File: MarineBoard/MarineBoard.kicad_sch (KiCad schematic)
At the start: 152 parts, among them CN1 MKDSN 1,5/ 2-5,08, CN2 MKDSN 1,5/ 2-5,08, CN3 SM04B-SRSS-TB (LF)(SN), J1 USB_C_Receptacle_USB2.0_16P, J3 Conn_02x09_Top_Bottom, Q1 IPL60R075CFD7, Q2 S8050, Q3 S8050, U1 SY8089A1AAC, U10 PC817C-S, U11 SN65HVD230DR, U12 DB125-3.5-3P-GN-S, U13 DB125-3.5-3P-GN-S, U14 PC817C-S, U15 TC4427EPA, U16 PC817C-S, U17 PC817C-S, U18 INA226, U19 INA226, U2 INA226, U20 SMAJ6.8CA, U3 TPS5430DDA, U4 DB125-3.5-2P-GN-S, U5 DB125-3.5-2P-GN-S, U6 DB125-3.5-2P-GN-S, U7 DB125-3.5-3P-GN-S, U8 ESP32-S3-WROOM-2-N32R16V, U9 DB125-3.5-3P-GN-S

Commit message: MarineBoard: schematic library/component update
Co-Authored-By: Claude Sonnet 5 <noreply@anthropic.com>
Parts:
- removed J3: Conn_02x09_Top_Bottom, Connector_PinHeader_1.27mm:PinHeader_2x09_P1.27mm_Vertical, symbol Connector_Generic:Conn_02x09_Top_Bottom
- added J2: DISP_QSPI_4IN_18P, EasyEDA:FH12-18S-0.5SH_QSPI4IN, symbol EasyEDA:DISP_QSPI_4IN_18P
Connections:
- net +3.3V: now also J2.17 (TP_VDD), J2.2 (VCI)
- net FSPIBL/GPIO18: now also J2.12 (FSPIBL)
- net FSPICLK/GPIO12: now also J2.5 (FSPICLK)
- net FSPICS0/GPIO10: now also J2.4 (FSPICS0)
- net FSPID/GPIO11: now also J2.6 (FSPID)
- net FSPIDC/GPIO21: now also J2.10 (FSPIDC)
- net FSPIHD/GPIO9: now also J2.8 (FSPIHD)
- net FSPIQ/GPIO13: now also J2.7 (FSPIQ)
- net FSPIRST/GPIO17: now also J2.3 (FSPIRST)
- net FSPITE/GPIO42: now also J2.11 (FSPITE)
- net FSPITI/GPIO47: now also J2.13 (FSPITI)
- net FSPIWP/GPIO14: now also J2.9 (FSPIWP)
- net GND: now also J2.1 (GND), J2.18 (GND)
- net GPIO3: now also J2.16 (TP_RST)
- net SCL: now also J2.15 (SCL)
- net SDA: now also J2.14 (SDA)

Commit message: MarineBoard: new from-scratch layout; Quilter-compatible footprints
- LCSC: nickname on all EasyEDA footprint lib IDs (board + schematic)
- EasyEDA.pretty upgraded to current KiCad format; 3D models moved to Lib/Models
- U10 FPC mounting tabs numbered 21/22 to match symbol
- L2 silkscreen arcs replaced with line segments (Quilter parser rejects fp_arc)

Co-Authored-By: Claude Opus 5.5 <noreply@anthropic.com>
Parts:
- removed C33: 1.2uF 100V, Capacitor_SMD:C_1210_3225Metric, symbol EasyEDA:HGC0402R5105K500NTEJ
- removed D14: MURS360T3G, EasyEDA:SMC_L7.1-W6.2-LS8.1-R-RD, symbol EasyEDA:MURS360T3G
- removed D5: 1N5819HW-7-F, EasyEDA:SMC_L7.1-W6.2-LS8.1-RD, symbol EasyEDA:1N5819HW-7-F
- removed D8: ESD5Z3.3T1G, EasyEDA:SOD-523_L1.2-W0.8-LS1.6-FD, symbol EasyEDA:ESD5Z3.3T1G_C2827729
- removed F2: 1A, EasyEDA:FUSE-TH_XF-506P, symbol EasyEDA:XF-506P
- removed H5: Jumper_Shunt, symbol Auxiliary_Items:Jumper_Shunt
- removed Q1: IPL60R075CFD7, EasyEDA:VSON-4_L8.1-W8.1-P2.00-BL, symbol EasyEDA:IPL60R075CFD7AUMA1-VB
- removed R17: 120, EasyEDA:R0805, symbol EasyEDA:0805W8F1200T5E
- removed R18: 10K, Resistor_SMD:R_0402_1005Metric, symbol Device:R
- removed R37: 100K, EasyEDA:R0805, symbol EasyEDA:0805W8F1003T5E_C149504
- removed R45: 2K2, EasyEDA:R2512, symbol EasyEDA:CRGP2512F2K2
- removed U10: PC817C-S, EasyEDA:SOP-4_L6.5-W4.6-P2.54-LS10.3-TL, symbol EasyEDA:PC817C-S
- removed U15: TC4427EPA, EasyEDA:DIP-8_L9.4-W6.4-P2.54-LS9.1-BL, symbol EasyEDA:TC4427EPA
- removed U20: SMAJ6.8CA, EasyEDA:SMA_L4.4-W2.6-LS5.0-BI, symbol EasyEDA:SMAJ6.8CA_C3001958
- added C33: 4.7uF, Capacitor_SMD:C_0402_1005Metric, symbol CL05A475MP5NRNC
- added C39: 1.2uF 100V, Capacitor_SMD:C_1210_3225Metric, symbol HGC0402R5105K500NTEJ
- added D14: SS56, Diode_SMD:D_SMA, symbol SS56_C18199169
- added D20: MBRS3100T3G, Diode_SMD:D_SMC, symbol MBRS3100T3G
- added D22: S3MB-13-F, Diode_SMD:D_SMB, symbol S3MB-13-F
- added D8: VS-43CTQ100S-M3, LCSC:D2PAK_L10.0-W9.0-P2.54-LS15.0-TL-1, symbol VS-43CTQ100S-M3
- added F2: 1A, LCSC:FUSE-TH_XF-506P, symbol XF-506P
- added H6, H7: MALE HEADER CONNECTOR, Connector_PinHeader_2.54mm:PinHeader_1x02_P2.54mm_Vertical, symbol HXPH254-01-02-Z-L11.5MALEHEADERCONNECTOR
- added Q4: BUK762R4-60E, LCSC:TO-263-2_L10.1-W9.1-P5.08-LS15.2-BR, symbol BUK762R4-60E,118-VB
- added R16, R46: 47K/1W, Resistor_SMD:R_2512_6332Metric, symbol CR2512F47KE04
- added R47: 2K2, Resistor_SMD:R_2512_6332Metric, symbol CRGP2512F2K2
- added R48: 10K, Resistor_SMD:R_0402_1005Metric, symbol Device:R
- added R49, R50: 120, Resistor_SMD:R_0805_2012Metric, symbol 0805W8F1200T5E
- added U10: 05A20L20P, LCSC:FPC-SMD_20P-P0.50_L5.9-W14.4, symbol 05A20L20P
- added U21: PC817C-S, LCSC:SOP-4_L6.5-W4.6-P2.54-LS10.3-TL, symbol PC817C-S
- added U22: SN74LVC1G14DBVR, Package_TO_SOT_SMD:SOT-23-5, symbol SN74LVC1G14DBVR
- added U23: MCP1407-E/MF_C640313, LCSC:DFN-8_L6.0-W5.0-P1.27-BL-EP4.0, symbol MCP1407-E_MF_C640313
- BUZZER1: footprint EasyEDA:BUZ-SMD_L4.0-W4.0-P3.50-L -> LCSC:BUZ-SMD_L4.0-W4.0-P3.50-L; symbol EasyEDA:KLJ-4020 -> KLJ-4020; LCSC Part C556936 -> (none)
- C1, C17, C25: LCSC Part C15525 -> (none)
- C10, C16, C30: symbol EasyEDA:CL05A475MP5NRNC -> CL05A475MP5NRNC; LCSC Part C23733 -> (none)
- C11, C12, C14, C19, C2, C22, C24, C27, C28, C3, C31, C32, C34, C35, C36, C37, C38, C5, C7, C9: LCSC Part C1525 -> (none)
- C13: symbol EasyEDA:01EC1809SHC10UF50V -> 01EC1809SHC10UF50V; LCSC Part C440198 -> (none)
- C15: symbol EasyEDA:RVT1V470M0605 -> RVT1V470M0605; LCSC Part C403725 -> (none)
- C18: symbol EasyEDA:CL05B103KB5NNNC -> CL05B103KB5NNNC; LCSC Part C15195 -> (none)
- C20: footprint EasyEDA:CAP-SMD_BD6.3-L6.6-W6.6-FD -> LCSC:CAP-SMD_BD6.3-L6.6-W6.6-FD; symbol EasyEDA:RVT1A221M0605-C72494 -> RVT1A221M0605-C72494; LCSC Part C125977 -> (none); MPN UWT1H221MNL1GS -> C125977
- C21: symbol EasyEDA:0603B152K500NT -> 0603B152K500NT; LCSC Part C668348 -> (none)
- C23: symbol EasyEDA:0603B151K500NT -> 0603B151K500NT; LCSC Part C76951 -> (none)
- C26, C29: symbol EasyEDA:CL10B473KB8NNNC -> CL10B473KB8NNNC; LCSC Part C368599 -> (none)
- C4, C8: symbol EasyEDA:CL21A226MAYNNNE -> CL21A226MAYNNNE; LCSC Part C3845593 -> (none); MPN GRM158R61A226ME15D -> C3845593
- C6: symbol EasyEDA:0603CG6R8C500NT -> 0603CG6R8C500NT; LCSC Part C88896 -> (none); MPN GJM1555C1H6R8BB01D -> C88896
- CN1, CN2: footprint EasyEDA:CONN-TH_2P-P5.08_1729128 -> LCSC:CONN-TH_2P-P5.08_1729128; symbol EasyEDA:1729128 -> 1729128; LCSC Part C7509570 -> (none)
- CN3: footprint EasyEDA:CONN-SMD_4P-P1.00_SM04B-SRSS-TB-LF-SN -> LCSC:CONN-SMD_4P-P1.00_SM04B-SRSS-TB-LF-SN; symbol EasyEDA:SM04B-SRSS-TB(LF)(SN) -> SM04B-SRSS-TB(LF)(SN); LCSC Part C160404 -> (none)
- D1, D15, D4: LCSC Part C2480 -> (none)
- D10: footprint EasyEDA:SOT-23-3_L2.9-W1.3-P1.90-LS2.4-BL-2 -> Package_TO_SOT_SMD:SOT-23; symbol EasyEDA:PESD1CAN_C2687121 -> PESD1CAN_C2687121; LCSC Part C2687121 -> (none); MPN (none) -> C2687121
- D11, D12, D13, D18, D19, D9: footprint EasyEDA:SOD-523_L1.2-W0.8-LS1.6-FD -> Diode_SMD:D_SOD-523; symbol EasyEDA:ESD5Z3.3T1G_C2827729 -> ESD5Z3.3T1G_C2827729; LCSC Part C2827729 -> (none)
- D16, D17: LCSC Part C2286 -> (none); MPN (none) -> C2286
- D2, D3: footprint EasyEDA:SOD-882_L1.0-W0.6-BI -> Diode_SMD:D_SOD-882; symbol L-3P1W836115A-altium-import:root_0_H5VL10B_ -> root_0_H5VL10B_; LCSC PART NAME 丝印 PB 双向ESD 5V截止 峰值浪涌电流：5A -> (none); Part Name (none) -> 丝印 PB 双向ESD 5V截止 峰值浪涌电流：5A; SUPPLIER LCSC -> JLC
- D6: footprint EasyEDA:SMB_L4.6-W3.6-LS5.3-RD -> Diode_SMD:D_SMB; symbol EasyEDA:SMBJ18A_C152104 -> SMBJ18A_C152104; LCSC Part C152104 -> (none)
- D7: footprint EasyEDA:SOD-123FL_L2.7-W1.8-LS3.8-RD -> Diode_SMD:D_SOD-123F; symbol EasyEDA:LMBR340FT1G -> LMBR340FT1G; LCSC Part C417538 -> (none); MPN (none) -> C417538
- F1, F3: footprint EasyEDA:FUSE-TH_XF-506P -> LCSC:FUSE-TH_XF-506P; symbol EasyEDA:XF-506P -> XF-506P; LCSC Part C492610 -> (none); MPN (none) -> C492610
- Flash1, Reset1: LCSC Part C318884 -> (none); MPN (none) -> C318884
- J1: footprint EasyEDA:USB_C_Receptacle_HCTL_HC-TYPE-C-16P-01A -> LCSC:USB_C_Receptacle_HCTL_HC-TYPE-C-16P-01A
- J2: footprint EasyEDA:FH12-18S-0.5SH_QSPI4IN -> LCSC:FH12-18S-0.5SH_QSPI4IN; symbol EasyEDA:DISP_QSPI_4IN_18P -> DISP_QSPI_4IN_18P
- JP1: symbol EasyEDA:1.27MM_1*2P -> 1.27MM_1*2P; LCSC Part C703015 -> (none); MPN (none) -> C703015
- L1: footprint EasyEDA:L2520 -> Inductor_SMD:L_1008_2520Metric; symbol EasyEDA:DFE252012F-1R0M=P2 -> DFE252012F-1R0M=P2; LCSC Part C435392 -> (none); MPN DFE252012F-1R0M=P2 -> C435392
- L10, L7, L9: footprint EasyEDA:L0805 -> Inductor_SMD:L_0805_2012Metric; symbol EasyEDA:BLM21PG331SN1D -> BLM21PG331SN1D; LCSC Part C74764 -> (none); MPN (none) -> C74764
- L2: footprint EasyEDA:IND-SMD_L12.5-W12.5_B82477P4XX -> LCSC:IND-SMD_L12.5-W12.5_B82477P4XX; symbol EasyEDA:FC-DR1207-101MT -> FC-DR1207-101MT; LCSC Part C5368704 -> (none); MPN (none) -> C5368704
- L3, L4, L6: footprint EasyEDA:L0805 -> Inductor_SMD:L_0805_2012Metric; symbol L-3P1W836115A-altium-import:root_0_BLM21PG121SN1D_ -> root_0_BLM21PG121SN1D_; LCSC PART NAME 单路 0805磁珠 阻抗120Ω@100MHz -> (none); Part Name (none) -> 单路 0805磁珠 阻抗120Ω@100MHz; SUPPLIER LCSC -> JLC
- L5: footprint EasyEDA:IND-SMD_L10.2-W10.0 -> LCSC:IND-SMD_L10.2-W10.0; symbol EasyEDA:CDRH104RNP-150NC -> CDRH104RNP-150NC; LCSC Part C225048 -> (none); MPN (none) -> C225048
- L8: footprint EasyEDA:FILTER-SMD_4P-L2.0-W1.2-BL_DLW21H -> LCSC:FILTER-SMD_4P-L2.0-W1.2-BL_DLW21H; symbol EasyEDA:DLW21SN900SQ2L -> DLW21SN900SQ2L; LCSC Part C97856 -> (none); MPN (none) -> C97856
- Q2, Q3: footprint EasyEDA:SOT-23-3_L2.9-W1.3-P1.90-LS2.3-BR -> Package_TO_SOT_SMD:SOT-23; symbol L-3P1W836115A-altium-import:root_0_S8050_C20069125_ -> root_0_S8050_C20069125_; LCSC PART NAME hFE:200-350，丝印:J3Y S8050 -> (none); Part Name (none) -> hFE:200-350，丝印:J3Y S8050; SUPPLIER LCSC -> JLC
- R1, R2: LCSC Part C25905 -> (none); MPN (none) -> C25905
- R10, R15, R20, R25, R26, R27, R28, R3, R32, R40, R42, R43: LCSC Part C25744 -> (none); MPN (none) -> C25744
- R11: footprint EasyEDA:R0201 -> Resistor_SMD:R_0201_0603Metric; symbol EasyEDA:PE0201FRF070R1L -> PE0201FRF070R1L; LCSC Part C2089436 -> (none); MPN (none) -> C2089436
- R12: footprint EasyEDA:R0402 -> Resistor_SMD:R_0402_1005Metric; symbol EasyEDA:0402WGF5901TCE -> 0402WGF5901TCE; LCSC Part C53159429 -> (none); MPN (none) -> C53159429
- R13: footprint EasyEDA:R0603 -> Resistor_SMD:R_0603_1608Metric; symbol EasyEDA:0603WAF5490T5E -> 0603WAF5490T5E; LCSC Part C23079 -> (none); MPN (none) -> C23079
- R14, R19, R21, R23, R24: footprint EasyEDA:R0805 -> Resistor_SMD:R_0805_2012Metric; symbol EasyEDA:0805W8F1200T5E -> 0805W8F1200T5E; LCSC Part C17437 -> (none); MPN (none) -> C17437
- R22, R29, R30, R41, R44: LCSC Part C11702 -> (none); MPN (none) -> C11702
- R31: footprint EasyEDA:R0805 -> Resistor_SMD:R_0805_2012Metric; symbol EasyEDA:0805W8F1000T5E -> 0805W8F1000T5E; LCSC Part C17408 -> (none); MPN (none) -> C17408
- R33, R34: LCSC Part C25117 -> (none); MPN (none) -> C25117
- R35, R36, R7, R9: footprint EasyEDA:R0805 -> Resistor_SMD:R_0805_2012Metric; symbol EasyEDA:FRC0805J100TS -> FRC0805J100TS; LCSC Part C2907296 -> (none); MPN (none) -> C2907296
- R38, R39: footprint EasyEDA:R0805 -> Resistor_SMD:R_0805_2012Metric; symbol EasyEDA:0805W8F470KT5E -> 0805W8F470KT5E; LCSC Part C48996903 -> (none); MPN (none) -> C48996903
- R4: footprint EasyEDA:R0805 -> Resistor_SMD:R_0805_2012Metric; symbol EasyEDA:0805W8F1003T5E_C149504 -> 0805W8F1003T5E_C149504; LCSC Part C149504 -> (none); MPN 0805W8F1003T5E -> C149504
- R5: LCSC Part C25105 -> (none); MPN (none) -> C25105
- R6: LCSC Part C25105 -> (none)
- R8: footprint EasyEDA:R0805 -> Resistor_SMD:R_0805_2012Metric; symbol EasyEDA:0805W8F2202T5E -> 0805W8F2202T5E; LCSC Part C17560 -> (none); MPN 0805W8F2202T5E -> C17560
- Relay1: footprint EasyEDA:RELAY-TH_SRD-XXVDC-XL-C -> LCSC:RELAY-TH_SRD-XXVDC-XL-C; symbol EasyEDA:SRD-12VDC-SL-C -> SRD-12VDC-SL-C; LCSC Part C30431 -> (none); MPN (none) -> C30431
- U1: footprint EasyEDA:TSOT-23-5_L2.9-W1.6-P0.95-LS2.8-BR -> Package_TO_SOT_SMD:TSOT-23-5; symbol EasyEDA:SY8089A1AAC -> SY8089A1AAC; LCSC Part C479074 -> (none); MPN SY8089A1AAC -> C479074
- U11: footprint EasyEDA:SOIC-8_L5.0-W4.0-P1.27-LS6.0-BL -> Package_SO:SOIC-8_3.9x4.9mm_P1.27mm; symbol EasyEDA:TJA1050T_CM,118 -> TJA1050T_CM,118; LCSC Part C12084 -> (none); MPN (none) -> C12084
- U12, U13, U7, U9: footprint EasyEDA:CONN-TH_3P-P3.50_L7.4-W10.5 -> LCSC:CONN-TH_3P-P3.50_L7.4-W10.5; symbol EasyEDA:DB125-3.5-3P-GN-S -> DB125-3.5-3P-GN-S; LCSC Part C466971 -> (none); MPN (none) -> C466971
- U14, U16, U17: footprint EasyEDA:SOP-4_L6.5-W4.6-P2.54-LS10.3-TL -> LCSC:SOP-4_L6.5-W4.6-P2.54-LS10.3-TL; symbol EasyEDA:PC817C-S -> PC817C-S; LCSC Part C3008369 -> (none); MPN (none) -> C3008369
- U18, U19: footprint EasyEDA:VSSOP-10_3x3mm_P0.5mm -> LCSC:VSSOP-10_3x3mm_P0.5mm; LCSC Part C2653835 -> (none)
- U2: footprint Package_SO:VSSOP-10_3x3mm_P0.5mm -> LCSC:VSSOP-10_3x3mm_P0.5mm; LCSC Part C2653835 -> (none)
- U3: LCSC Part C502477 -> (none); MPN (none) -> C502477
- U4, U5, U6: footprint EasyEDA:CONN-TH_2P-P3.50_L7.4-W7.0 -> LCSC:CONN-TH_2P-P3.50_L7.4-W7.0; symbol EasyEDA:DB125-3.5-2P-GN-S -> DB125-3.5-2P-GN-S; LCSC Part C466970 -> (none); MPN (none) -> C466970
- U8: footprint PCM_Espressif:ESP32-S3-WROOM-2 -> RF_Module:ESP32-S3-WROOM-2; symbol PCM_Espressif:ESP32-S3-WROOM-2 -> ESP32-S3-WROOM-2; LCSC Part C42417293 -> (none); MPN (none) -> C42417293
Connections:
- net +12V BAT: now also C33.2, D14.2 (A), D8.2 (-), U23.1 (VDD), U23.8 (VDD)
- net +3.3V: now also U10.1, U21.4, U22.5 (VCC); no longer J2.2 (VCI)
- net FSPICLK/GPIO12: now also U10.3; no longer J2.5 (FSPICLK)
- net FSPICS0/GPIO10: now also U10.6; no longer J2.4 (FSPICS0)
- net FSPICS1/GPIO39: now also H6.1
- net FSPIRST/GPIO17: now also U10.8; no longer J2.3 (FSPIRST)
- net GND: now also C33.1, D20.2 (A), D22.2, Q4.3 (S), R46.1, R48.2, U10.2, U21.2, U22.3 (GND), U23.4 (GND), U23.5 (GND), U23.9 (EP); no longer J2.1 (GND)
- net GPIO16: now also H6.2
- net GPIO5: now also H7.1
- net GPIO6: now also H7.2
- net PWM1_DRIVE: now also D8.1 (+), D8.3 (+), Q4.2 (D)
- net RPM_GPIO: now also R49.2
- net SH+: no longer U13.2
- net at C18.1, D7.1 (C), L5.1: now also U3.8 (PH)
- net at D4.2 (A): now also F2.2; no longer L6.2
- net at R40.1: now also Q4.1 (G), U23.6 (OUT), U23.7 (OUT)
- net at R32.1, U16.3: now also R50.2
- net at F1.1: now also D14.1 (K)
- new net: D20.1 (C), R16.1, R46.2, R47.1
- new net: D22.1, R47.2, U21.1
- new net: C39.2, R16.2
- new net: R48.1, U21.3, U22.2 (A)
- new net: R49.1, U22.4 (Y)
- new net: F2.1, L6.2
- new net: R50.1, U23.2 (INPUT)
- new net RPM: C39.1, U13.2
- no-connect marks 12 -> 10
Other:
- note added: "PWM DRIVER"
- note removed: "PWM DRIVERS"
- moved on the sheet: C36, D12, D15, F3, H1, H2, H3, H4, J2, Q2, R22, R23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

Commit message: MarineBoard: fix decoupling and capacitor ratings/footprints
- ESP32: add C40 10uF + C41 0.1uF on new ESP_3V3 net (U8 side of ferrite L7,
  which previously had no local decoupling)
- U23 gate driver: add C42 0.1uF/50V at VDD
- C16/C17 on 12V buck input: 10V/6.3V 0402 parts -> 50V 1206
  (CL31B475KBHNNNE, CL31A106KBHNNNE)
- C18/C21/C23/C26/C29: 01005 footprint -> 0402 to match their 0402 MPNs
- C20: part fields aligned with 6.3mm footprint (RVT1A221M0605, 220uF 10V)

Board needs Update PCB from Schematic (F8) to pick up footprint changes.

Co-Authored-By: Claude Opus 5.5 <noreply@anthropic.com>
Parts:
- added C40: 10uF, Capacitor_SMD:C_0603_1608Metric, symbol Device:C
- added C41, C42: 0.1uF, Capacitor_SMD:C_0402_1005Metric, symbol Device:C
- C16: footprint Capacitor_SMD:C_0402_1005Metric -> Capacitor_SMD:C_1206_3216Metric; MPN CL05A475MP5NRNC -> (none); Package 0402 -> 1206
- C17: footprint Capacitor_SMD:C_0402_1005Metric -> Capacitor_SMD:C_1206_3216Metric; MPN CL05A106MQ5NUNC -> (none); Package 0402 -> 1206
- C18, C21, C23, C26, C29: footprint Capacitor_SMD:C_01005_0402Metric -> Capacitor_SMD:C_0402_1005Metric
- C20: MPN C125977 -> C72494; Manufacturer Nichicon -> Lelon; Package SMD,D10xL10mm -> SMD,D6.3xL5.4mm
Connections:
- net +12V BAT: now also C42.1
- net GND: now also C40.2, C41.2, C42.2
- net ESP_3V3: now reaches L7.1, U8.2 (3V3)
- net ESP_3V3: now also C40.1, C41.1

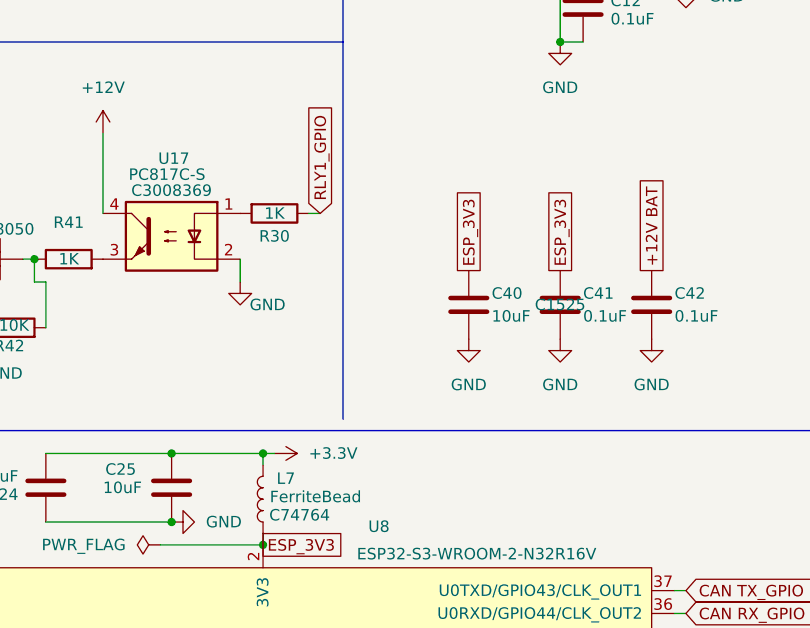
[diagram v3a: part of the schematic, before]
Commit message: MarineBoard: ESP32 decoupling on correct side of ferrite L7
C24/C25 were drawn as the ESP32 decoupling but wired to the +3.3V side of
ferrite bead L7, leaving U8's 3V3 pin with no local capacitance. Rewire them
onto ESP_3V3 (U8 side of L7) and drop the interim C40/C41 duplicates.
C42 (U23 VDD) stays.

Board: saved after Update PCB from Schematic (cap footprint fixes applied);
needs one more F8 to drop C40/C41 and move C24/C25 to ESP_3V3.

Co-Authored-By: Claude Opus 5.5 <noreply@anthropic.com>
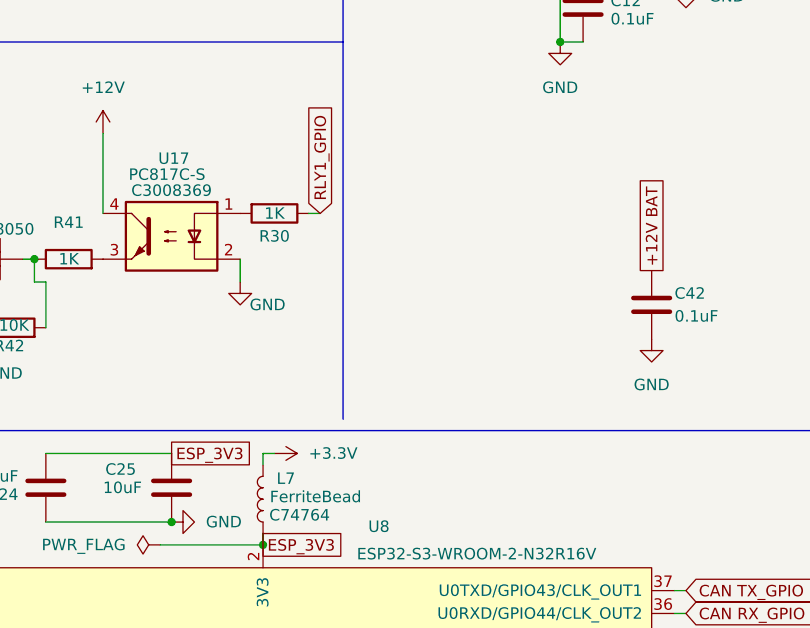
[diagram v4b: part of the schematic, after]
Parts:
- removed C40: 10uF, Capacitor_SMD:C_0603_1608Metric, symbol Device:C
- removed C41: 0.1uF, Capacitor_SMD:C_0402_1005Metric, symbol Device:C
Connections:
- net +3.3V: no longer C24.2, C25.1
- net ESP_3V3: now also C24.2, C25.1

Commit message: MarineBoard: routed 4-layer board, PCBWay fab package, spec v1.8 (#178)
Board
- Fuses sized to copper: F1 2 A, F3 10 A, new F4 10 A on relay common
- CN2 label fixed (PWM1 vs PWM split left the field open)
- Power nets named; net classes <ROLE>_<V>_<A>; MarineBoard.kicad_dru
  current-width rules + PCBWay-only limits; board rules = stricter of
  project vs PCBWay (clearance 0.127, ring 0.15, hole-to-hole 0.28 ...)
- Edge.Cuts 83.0 x 67.5 mm; duplicate vias removed; GND stitching,
  Q4-source and D8 thermal via arrays; vias moved out of small pads
- U10 (SM10B-GHS-TB) consolidated into Lib/EasyEDA (LCSC lib); stray
  root EasyEDA library removed

Fab / docs
- production/: 4-layer Gerbers + drill + IPC-D-356, zip, BOM, positions
- PCBWay spec sheet: size, ENIG, 1 oz outer, thermal-via plugging note
- Technical Specs v1.8: U10 display header replaces J3/J2/H6/H7,
  Mechanical & fabrication section; Documentation PNGs re-exported
- quilter_nets.py regenerates the Quilter high-current CSV from classes

Co-Authored-By: Claude Opus 5.5 <noreply@anthropic.com>
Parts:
- removed H6, H7: MALE HEADER CONNECTOR, Connector_PinHeader_2.54mm:PinHeader_1x02_P2.54mm_Vertical, symbol HXPH254-01-02-Z-L11.5MALEHEADERCONNECTOR
- removed J2: DISP_QSPI_4IN_18P, LCSC:FH12-18S-0.5SH_QSPI4IN, symbol DISP_QSPI_4IN_18P
- removed U10: 05A20L20P, LCSC:FPC-SMD_20P-P0.50_L5.9-W14.4, symbol 05A20L20P
- added F4: 10A, LCSC:FUSE-TH_XF-506P, symbol XF-506P
- added U10: SM10B-GHS-TB, LCSC:CONN-SMD_SM10B-GHS-TB, symbol LCSC:SM10B-GHS-TB
- F1: value 5A -> 2A
- F3: value 15A -> 10A
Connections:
- net +12V: now also U5.1; no longer U5.2
- net +3.3V: now also U10.1
- net +5V: now also U10.10
- net CANH: now also U7.1; no longer U7.2
- net CANL: now also U7.2; no longer U7.1
- net CO1: now also F4.1; no longer Relay1.5
- net GND: now also U10.11, U10.12, U10.2
- net LVL1: now also U5.2; no longer U5.1
- net SW_5V: now reaches C18.1, D7.1 (C), L5.1, U3.8 (PH)
- net SW_3V3: now reaches L1.1, U1.3 (LX)
- net 5V_FUSED: now reaches D4.2 (A), F2.2
- net VIN_FUSED: now reaches C19.1, D6.1 (C), F1.2, L2.1
- net VIN_FILT: now reaches C15.1, L2.2, L3.1
- net VIN_BUCK: now reaches C16.2, C17.1, L3.2, L4.1, U3.5 (EN), U3.7 (VIN)
- net VIN_RP: now reaches D14.1 (K), F1.1
- net VBUS: now reaches C1.1, C7.1, D1.2 (A), J1.A4 (VBUS), J1.A9 (VBUS), J1.B4 (VBUS), J1.B9 (VBUS)
- net PWM_GATE: now reaches Q4.1 (G), R40.1, U23.6 (OUT), U23.7 (OUT)
- net 5V_BUCK: now reaches C20.1, C21.2, L5.2, L6.1, R10.2
- net 5V_FILT: now reaches F2.1, L6.2
- net FSPIBL/GPIO18 renamed BL/GPIO18
- net BL/GPIO18: now also U10.9
- net FSPICLK/GPIO12 renamed SCK/GPIO12
- net SCK/GPIO12: now also U10.3
- net FSPICS0/GPIO10 renamed CS0/GPIO10
- net CS0/GPIO10: now also U10.6
- net FSPICS1/GPIO39: no longer names the net of U8.32 (MTCK/GPIO39/CLK_OUT3/SUBSPICS1)
- net FSPID/GPIO11 renamed MOSI/GPIO11
- net MOSI/GPIO11: now also U10.4
- net FSPIDC/GPIO21: no longer names the net of U8.23 (GPIO21)
- net FSPIHD/GPIO9 renamed DC/GPIO9
- net DC/GPIO9: now also U10.7
- net FSPIQ/GPIO13 renamed MISO/GPIO13
- net MISO/GPIO13: now also U10.5
- net FSPIRST/GPIO17: no longer names the net of U8.10 (GPIO17/U1TXD/ADC2_CH6)
- net FSPITE/GPIO42: no longer names the net of U8.35 (MTMS/GPIO42)
- net FSPITI/GPIO47: no longer names the net of U8.24 (GPIO47/SPICLK_P/SUBSPICLK_P_DIFF)
- net FSPIWP/GPIO14 renamed RST/GPIO14
- net RST/GPIO14: now also U10.8
- net GPIO16: no longer names the net of U8.9 (GPIO16/U0CTS/ADC2_CH5/XTAL_32K_N)
- net GPIO3: no longer names the net of U8.15 (GPIO3/TOUCH3/ADC1_CH2)
- net GPIO5: no longer names the net of U8.5 (GPIO5/TOUCH5/ADC1_CH4)
- net GPIO6: no longer names the net of U8.6 (GPIO6/TOUCH6/ADC1_CH5)
- net PWM1 renamed PWM
- net PWM1_DRIVE renamed PWM_DRIVE
- new net RLY1_COM: F4.2, Relay1.5
- no-connect marks 10 -> 19

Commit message: MarineBoard: RPM input sized for phase-lead tap (#26)
R16 47k -> 10k 1W (25121WF1002T4E), R48 10k -> 47k (C25792); same
footprints, Gerbers unchanged. With the 47k/47k divider the PC817 got
~0.1 mA from a +/-7.5 V AC-coupled phase signal - no reliable pulses.
Now ~0.5 mA, U22 saturates; 100 V fault ~4 mA LED / 0.15 W in R16.

BOM + positions regenerated. INSTALLATION 6.3.7 (v1.10): rev 2 taps a
phase lead, as-built circuit table; Technical Specs RPM row.

Co-Authored-By: Claude Opus 5.5 <noreply@anthropic.com>
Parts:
- R16: value 47K/1W -> 10K/1W; MPN C175364 -> 25121WF1002T4E
- R48: value 10K -> 47K; MPN C25744 -> C25792
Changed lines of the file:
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@@
 			)
 		)
-		(property "Value" "10K"
+		(property "Value" "47K"
 			(at 219.71 185.42 90)
 			(show_name no)
@@
 			)
 		)
-		(property "MPN" "C25744"
+		(property "MPN" "C25792"
 			(at 219.71 185.42 90)
 			(hide yes)
@@
 			)
 		)
-		(property "Value" "47K/1W"
+		(property "Value" "10K/1W"
 			(at 172.466 168.402 0)
 			(show_name no)
@@
 			)
 		)
-		(property "MPN" "C175364"
+		(property "MPN" "25121WF1002T4E"
 			(at 174.498 169.418 0)
 			(show_name no)
